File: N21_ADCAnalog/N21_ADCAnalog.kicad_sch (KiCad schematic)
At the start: 53 parts

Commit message: Updates, add N25
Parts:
- added C2101: 10n, Capacitor_THT:C_Disc_D4.3mm_W1.9mm_P5.00mm, symbol Device:C
- added C2102, C2107, C2108, C2109: 22n, Capacitor_THT:C_Disc_D4.3mm_W1.9mm_P5.00mm, symbol Device:C
- added C2114, C2117: 6u8, Capacitor_THT:C_Disc_D5.0mm_W2.5mm_P5.00mm, symbol Device:C
- added C2115, C2116: 22u, Capacitor_THT:C_Disc_D5.0mm_W2.5mm_P5.00mm, symbol Device:C
- added unit 5 of D2101
- added TP2103: 0Vref, Connector_Pin:Pin_D1.0mm_L10.0mm, symbol Connector:TestPoint
- A2102: symbol Amplifier_Operational:AD8021ARM -> Amplifier_Operational:LM201
- K1: footprint Philips_PM2528:PM2528_RiserCardConnector -> PM2528:PM2528_RiserCardConnector
- R2119: footprint Package_DIP:DIP-16_W7.62mm -> Package_DIP:DIP-14_W7.62mm_Socket
- V2101: symbol PM2528:ON528 -> PM2528:FET_Dual
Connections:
- net +15V: now also C2101.2, C2107.1, C2114.1
- net +5V: now also C2115.1
- net -15V: now also C2102.2, C2108.2, C2117.2
- net -5V: now also C2109.2, C2116.2, D2101.7 (VSS)
- net GND3: now also TP2103.1
- net GND4: now also C2101.1, C2102.1, C2107.2, C2108.1, C2109.1, C2114.2, C2115.2, C2116.1, C2117.1, D2101.14 (VDD)
- net at R2106.1, V2101.4 (2S): no longer A2102.3 (+)
- net at A2102.6, C2103.1, R2109.1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: now also A2102.1 (BAL), C2105.1
- net at R2105.1, V2101.1 (1S): no longer A2102.2 (-)
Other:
- removed sheet Powerrails
- note added: "Measuring zero"
- note added: "Power"
- note added: "Supply zero"
- title: PM2528 N21 (ADC Analog) | Power -> Philips PM2528 - N21 (ADC Analog)
- moved on the sheet: C2105, D2102, R2116, TP2105

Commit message: Small updates, N25 also
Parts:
- R2104, R2115, R2118, R2121: footprint Potentiometer_THT:Potentiometer_Bourns_3296Y_Vertical -> PM2528:Potentiometer horizontal ceramic
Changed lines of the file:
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@@
 			)
 		)
-		(property "Footprint" "Potentiometer_THT:Potentiometer_Bourns_3296Y_Vertical"
+		(property "Footprint" "PM2528:Potentiometer horizontal ceramic"
 			(at 259.08 100.33 0)
 			(effects
@@
 			)
 		)
-		(property "Footprint" "Potentiometer_THT:Potentiometer_Bourns_3296Y_Vertical"
+		(property "Footprint" "PM2528:Potentiometer horizontal ceramic"
 			(at 152.4 93.98 0)
 			(effects
@@
 			)
 		)
-		(property "Footprint" "Potentiometer_THT:Potentiometer_Bourns_3296Y_Vertical"
+		(property "Footprint" "PM2528:Potentiometer horizontal ceramic"
 			(at 124.46 142.24 0)
 			(effects
@@
 			)
 		)
-		(property "Footprint" "Potentiometer_THT:Potentiometer_Bourns_3296Y_Vertical"
+		(property "Footprint" "PM2528:Potentiometer horizontal ceramic"
 			(at 74.93 128.27 0)
 			(effects

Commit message: Update schematics, move projectlibraries to D:
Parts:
- added JP1, JP2, JP3, JP4: Jumper_2_Small_Bridged, TestPoint:TestPoint_Bridge_Pitch2.54mm_Drill1.0mm, symbol Jumper:Jumper_2_Small_Bridged
- A2104: footprint (none) -> Package_DIP:DIP-8_W7.62mm
- C2101: value 10n -> 10n/100V
- C2102, C2107, C2108, C2109: value 22n -> 22n/63V
- C2103: value 162n -> 162n/100V
- C2104: value 3u3 -> 3u3/100V
- C2105, C2112, C2113: value 33p -> 33p/100V
- C2106: value 220p -> 220p/500V
- C2110: value 4n7 -> 4n7/100V
- C2111: value 4n22 -> 4n22/63V; footprint (none) -> Capacitor_THT:C_Axial_L5.1mm_D3.1mm_P15.00mm_Horizontal
- C2114, C2117: value 6u8 -> 6u8/25V
- C2115, C2116: value 22u -> 22u/10V
- R2119: value ~ -> OM528
- R2120: value ~ -> 590; footprint (none) -> Resistor_THT:R_Axial_DIN0309_L9.0mm_D3.2mm_P12.70mm_Horizontal
- V2101: footprint (none) -> Package_TO_SOT_THT:TO-78-6
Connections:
- net at R2106.1, V2101.4 (2S): now also A2102.3 (+)
- net at R2118.1, R2119.5: now also JP4.2 (B); no longer R2119.11
- net at R2105.1, V2101.1 (1S): now also A2102.2 (-)
- new net: JP1.2 (B), R2119.1, R2120.1
- new net: JP2.2 (B), JP3.1 (A), R2119.2
- new net: JP3.2 (B), R2119.13
- new net: JP1.1 (A), JP2.1 (A), R2119.14
- new net: JP4.1 (A), R2119.11
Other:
- note added: "A"
- note added: "B"
- note added: "C"
- note added: "D"
- moved on the sheet: A2101, A2102, A2103, A2104, A2105, A2106, C2101, C2102, C2103, C2104, C2105, C2106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

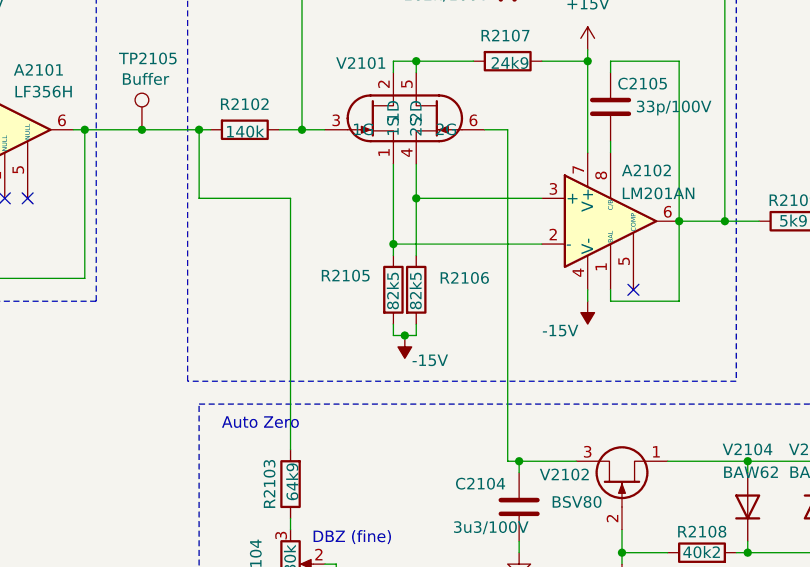
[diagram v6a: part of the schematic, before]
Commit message: Restructure folders, added EPROM-dumps
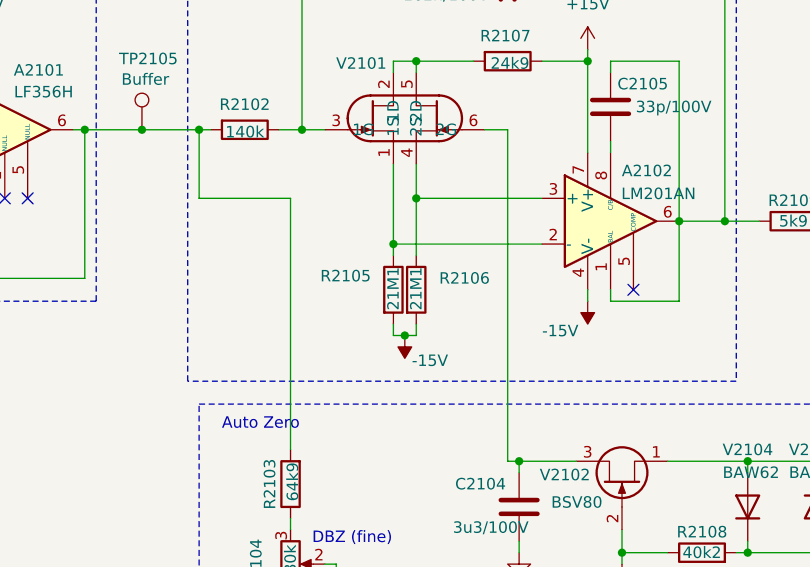
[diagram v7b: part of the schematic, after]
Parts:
- R2105, R2106: value 82k5 -> 21M1
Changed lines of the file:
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@@
 	(title_block
 		(title "Philips PM2528 - N21 (ADC Analog)")
-		(date "2025-07-06")
+		(date "2025-07-22")
 		(rev "1.0")
 	)
@@
 			)
 		)
-		(property "Value" "82k5"
+		(property "Value" "21M1"
 			(at 175.26 65.786 90)
 			(effects
@@
 			)
 		)
-		(property "Value" "82k5"
+		(property "Value" "21M1"
 			(at 172.72 65.786 90)
 			(effects
@@
 					(size 1.27 1.27)
 				)
+				(hide yes)
 			)
 		)
